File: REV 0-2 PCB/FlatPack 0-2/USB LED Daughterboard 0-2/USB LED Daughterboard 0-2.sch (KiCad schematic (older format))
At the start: 59 parts, among them J1 USB_C_Receptacle_USB2.0, J2 Conn_02x05_Odd_Even, Q1 SQJ479EP, U1 STUSB4500, U2 PCA9685PW

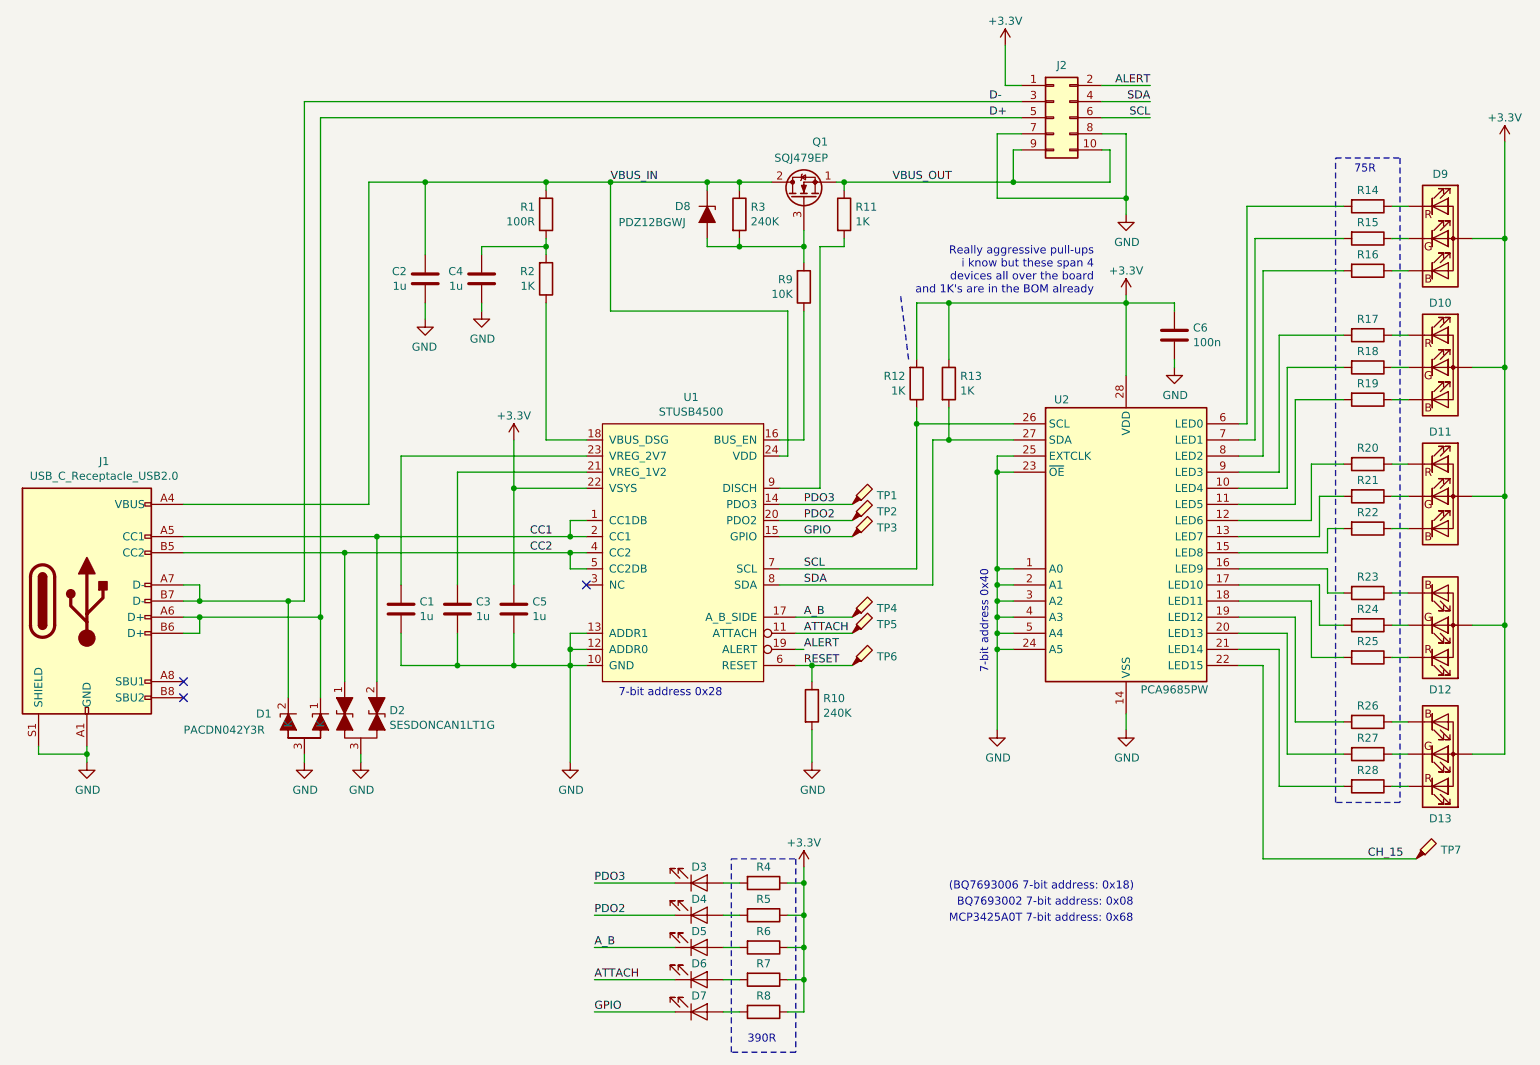
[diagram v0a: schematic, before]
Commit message: Finishing USB LED Daughterboard
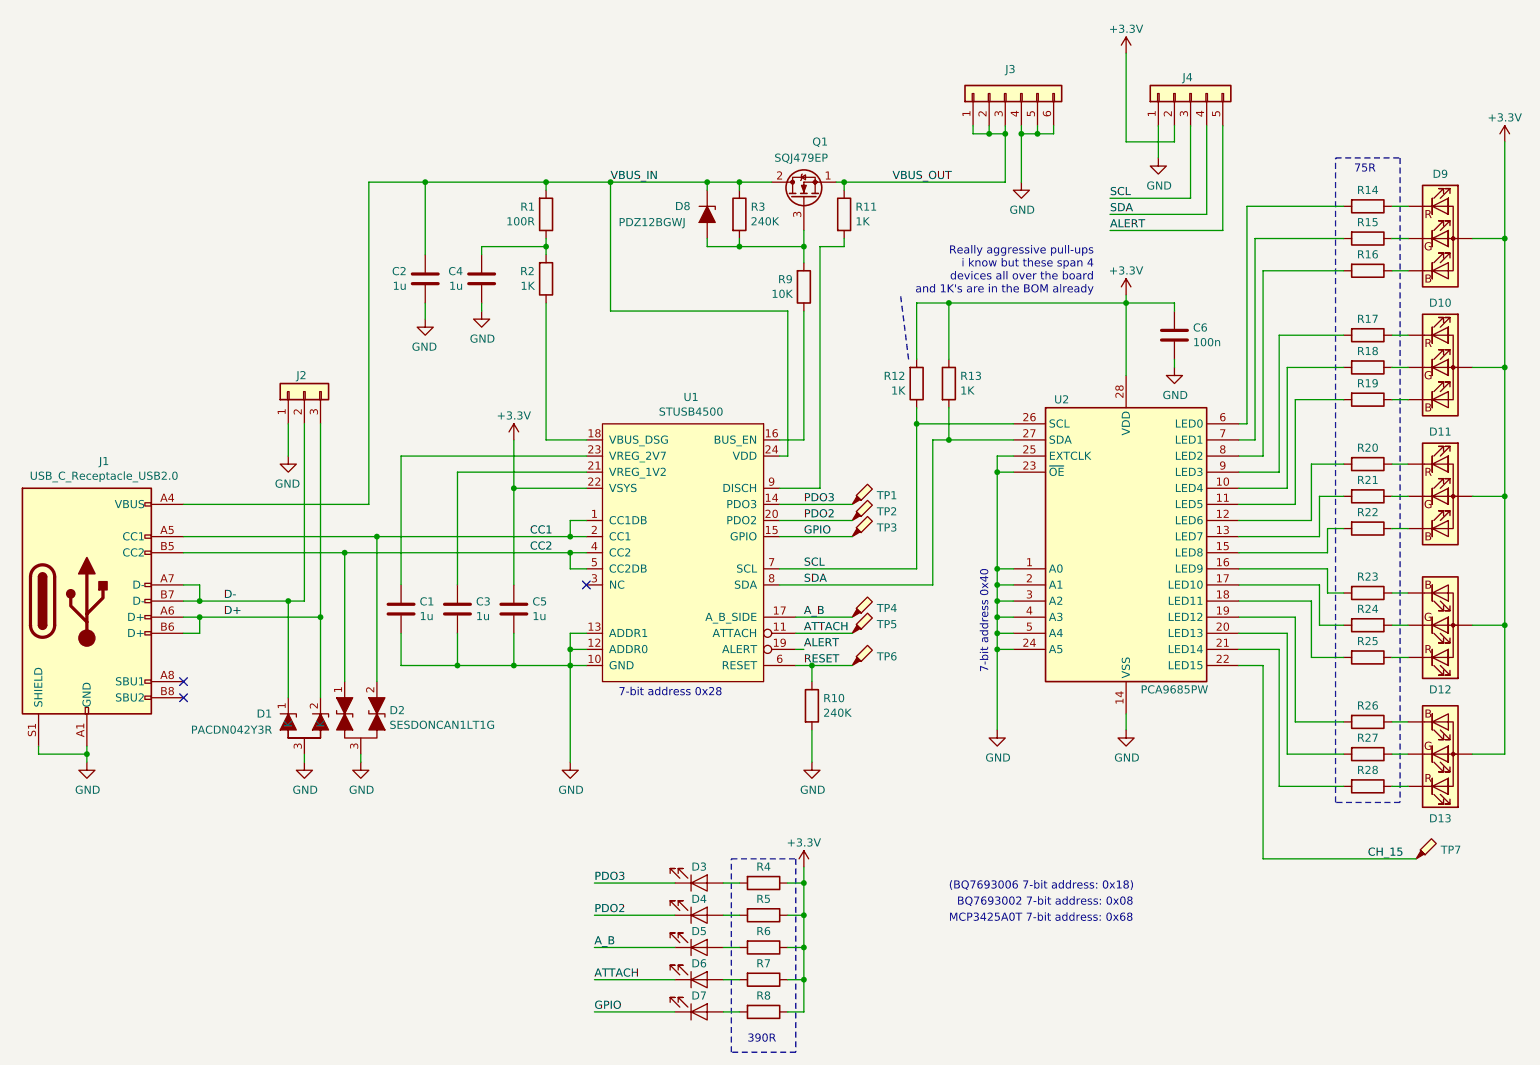
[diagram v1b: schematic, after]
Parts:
- removed J2: Conn_02x05_Odd_Even, Connector_PinHeader_2.54mm:PinHeader_2x05_P2.54mm_Vertical, symbol Connector_Generic:Conn_02x05_Odd_Even
- added J2: Conn_01x03, Connector_PinHeader_2.54mm:PinHeader_1x03_P2.54mm_Vertical, symbol Connector_Generic:Conn_01x03
- added J3: Conn_01x06, Connector_PinHeader_2.54mm:PinHeader_1x06_P2.54mm_Vertical, symbol Connector_Generic:Conn_01x06
- added J4: Conn_01x05, Connector_PinHeader_2.54mm:PinHeader_1x05_P2.54mm_Vertical, symbol Connector_Generic:Conn_01x05
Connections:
- net +3V3: now also J4.2 (Pin_2)
- net ALERT: now also J4.5 (Pin_5)
- net D+: now also D1.2 (K), J2.3 (Pin_3); no longer D1.1 (K)
- net D-: now also D1.1 (K), J2.2 (Pin_2); no longer D1.2 (K)
- net GND: now also J2.1 (Pin_1), J3.4 (Pin_4), J3.5 (Pin_5), J3.6 (Pin_6), J4.1 (Pin_1)
- net SCL: now also J4.3 (Pin_3)
- net SDA: now also J4.4 (Pin_4)
- net VBUS_OUT: now also J3.1 (Pin_1), J3.2 (Pin_2), J3.3 (Pin_3)
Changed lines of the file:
@@
 EESchema Schematic File Version 4
 LIBS:USB LED Daughterboard 0-2-cache
-EELAYER 29 0
+EELAYER 30 0
 EELAYER END
 $Descr A4 11693 8268
@@
 	2350 4700 2250 4700
 $Comp
-L power:GND #PWR03
+L power:GND #PWR04
 U 1 1 5DA9B4FB
 P 3350 5500
-F 0 "#PWR03" H 3350 5250 50  0001 C CNN
+F 0 "#PWR04" H 3350 5250 50  0001 C CNN
 F 1 "GND" H 3355 5327 50  0000 C CNN
 F 2 "" H 3350 5500 50  0001 C CNN
@@
 $EndComp
 $Comp
-L power:GND #PWR07
+L power:GND #PWR08
 U 1 1 5DA9C260
 P 4650 5500
-F 0 "#PWR07" H 4650 5250 50  0001 C CNN
+F 0 "#PWR08" H 4650 5250 50  0001 C CNN
 F 1 "GND" H 4655 5327 50  0000 C CNN
 F 2 "" H 4650 5500 50  0001 C CNN
@@
 	4500 3500 4500 2650
 $Comp
-L power:+3.3V #PWR06
+L power:+3.3V #PWR07
 U 1 1 5DA981B9
 P 4300 3500
-F 0 "#PWR06" H 4300 3350 50  0001 C CNN
+F 0 "#PWR07" H 4300 3350 50  0001 C CNN
 F 1 "+3.3V" H 4300 3650 50  0000 C CNN
 F 2 "" H 4300 3500 50  0001 C CNN
@@
 	10450 2250 10450 3050
 $Comp
-L power:+3.3V #PWR016
+L power:+3.3V #PWR018
 U 1 1 5DB37E24
 P 10450 1650
-F 0 "#PWR016" H 10450 1500 50  0001 C CNN
+F 0 "#PWR018" H 10450 1500 50  0001 C CNN
 F 1 "+3.3V" H 10450 1800 50  0000 C CNN
 F 2 "" H 10450 1650 50  0001 C CNN
@@
 CH_15
 $Comp
-L power:+3.3V #PWR013
+L power:+3.3V #PWR014
 U 1 1 5DB4EEEE
 P 8100 2600
-F 0 "#PWR013" H 8100 2450 50  0001 C CNN
+F 0 "#PWR014" H 8100 2450 50  0001 C CNN
 F 1 "+3.3V" H 8100 2750 50  0000 C CNN
 F 2 "" H 8100 2600 50  0001 C CNN
@@
 	8100 2650 8100 3100
 $Comp
-L power:GND #PWR015
+L power:GND #PWR017
 U 1 1 5DB5ADE0
 P 8400 3050
-F 0 "#PWR015" H 8400 2800 50  0001 C CNN
+F 0 "#PWR017" H 8400 2800 50  0001 C CNN
 F 1 "GND" H 8405 2877 50  0000 C CNN
 F 2 "" H 8400 3050 50  0001 C CNN
@@
 	8400 3000 8400 3050
 $Comp
-L power:GND #PWR014
+L power:GND #PWR015
 U 1 1 5DB69830
 P 8100 5300
-F 0 "#PWR014" H 8100 5050 50  0001 C CNN
+F 0 "#PWR015" H 8100 5050 50  0001 C CNN
 F 1 "GND" H 8105 5127 50  0000 C CNN
 F 2 "" H 8100 5300 50  0001 C CNN
@@
 	8100 5200 8100 5300
 $Comp
-L power:GND #PWR010
+L power:GND #PWR011
 U 1 1 5DB6DFF4
 P 7300 5300
-F 0 "#PWR010" H 7300 5050 50  0001 C CNN
+F 0 "#PWR011" H 7300 5050 50  0001 C CNN
 F 1 "GND" H 7305 5127 50  0000 C CNN
 F 2 "" H 7300 5300 50  0001 C CNN
@@
 	4100 2700 4100 2650
 $Comp
-L power:GND #PWR05
+L power:GND #PWR06
 U 1 1 5DC4C96E
 P 4100 2700
-F 0 "#PWR05" H 4100 2450 50  0001 C CNN
+F 0 "#PWR06" H 4100 2450 50  0001 C CNN
 F 1 "GND" H 4105 2527 50  0000 C CNN
 F 2 "" H 4100 2700 50  0001 C CNN
@@
 	3750 2750 3750 2650
 $Comp
-L power:GND #PWR04
+L power:GND #PWR05
 U 1 1 5DC257E0
 P 3750 2750
-F 0 "#PWR04" H 3750 2500 50  0001 C CNN
+F 0 "#PWR05" H 3750 2500 50  0001 C CNN
 F 1 "GND" H 3755 2577 50  0000 C CNN
 F 2 "" H 3750 2750 50  0001 C CNN
@@
 Wire Notes Line
 	6750 3000 6700 2600
-Text Notes 7900 2600 2    50   ~ 0
-Really aggressive pull-ups\ni know but these span 4 \ndevices all over the board\nand 1K's are in the BOM already
 $Comp
 L Device:D_Zener_ALT D8
@@
 	6150 4900 6150 5000
 $Comp
-L power:GND #PWR09
+L power:GND #PWR010
 U 1 1 5DE6D938
 P 6150 5500
-F 0 "#PWR09" H 6150 5250 50  0001 C CNN
+F 0 "#PWR010" H 6150 5250 50  0001 C CNN
 F 1 "GND" H 6155 5327 50  0000 C CNN
 F 2 "" H 6150 5500 50  0001 C CNN
@@
 U 1 1 5DF6EEEB
 P 3000 5350
-F 0 "D1" H 3300 5500 50  0000 R CNN
-F 1 "PACDN042Y3R" H 3750 5400 50  0000 R CNN
+F 0 "D1" H 2800 5500 50  0000 R CNN
+F 1 "PACDN042Y3R" H 2800 5400 50  0000 R CNN
 F 2 "Package_TO_SOT_SMD:SOT-23" H 3000 5350 50  0001 C CNN
 F 3 "https://www.onsemi.com/pub/Collateral/PACDN042-D.PDF" H 3000 5350 50  0001 C CNN
 	1    3000 5350
-	-1   0    0    -1
+	1    0    0    -1
 $EndComp
 Wire Wire Line
@@
 	3000 5500 3000 5450
 $Comp
-L power:GND #PWR02
+L power:GND #PWR03
 U 1 1 5DFAE1CC
 P 3000 5500
-F 0 "#PWR02" H 3000 5250 50  0001 C CNN
+F 0 "#PWR03" H 3000 5250 50  0001 C CNN
 F 1 "GND" H 3005 5327 50  0000 C CNN
 F 2 "" H 3000 5500 50  0001 C CNN
@@
 $EndComp
 $Comp
-L power:+3.3V #PWR08
+L power:+3.3V #PWR09
 U 1 1 5DFBA3DA
 P 6100 6150
-F 0 "#PWR08" H 6100 6000 50  0001 C CNN
+F 0 "#PWR09" H 6100 6000 50  0001 C CNN
 F 1 "+3.3V" H 6100 6300 50  0000 C CNN
 F 2 "" H 6100 6150 50  0001 C CNN
@@
 GPIO
 Wire Wire Line
-	6350 1900 7400 1900
-Connection ~ 6350 1900
-$Comp
-L Connector_Generic:Conn_02x05_Odd_Even J2
-U 1 1 5E0D0712
-P 7650 1500
-F 0 "J2" H 7700 1825 50  0000 C CNN
-F 1 "Conn_02x05_Odd_Even" H 7700 1826 50  0001 C CNN
-F 2 "Connector_PinHeader_2.54mm:PinHeader_2x05_P2.54mm_Vertical" H 7650 1500 50  0001 C CNN
-F 3 "~" H 7650 1500 50  0001 C CNN
-	1    7650 1500
-	1    0    0    -1
-$EndComp
-Wire Wire Line
-	7950 1700 8000 1700
-Wire Wire Line
-	8000 1700 8000 1900
-Wire Wire Line
-	7450 1700 7400 1700
-Wire Wire Line
-	7400 1700 7400 1900
-Connection ~ 7400 1900
-Wire Wire Line
-	7400 1900 8000 1900
-Wire Wire Line
-	7450 1600 7300 1600
-Wire Wire Line
-	7300 1600 7300 2000
-Wire Wire Line
-	7300 2000 8100 2000
-Wire Wire Line
-	8100 2000 8100 1600
-Wire Wire Line
-	8100 1600 7950 1600
-$Comp
-L power:GND #PWR012
-U 1 1 5E1029DF
-P 8100 2100
-F 0 "#PWR012" H 8100 1850 50  0001 C CNN
-F 1 "GND" H 8105 1927 50  0000 C CNN
-F 2 "" H 8100 2100 50  0001 C CNN
-F 3 "" H 8100 2100 50  0001 C CNN
-	1    8100 2100
-	1    0    0    -1
-$EndComp
-Wire Wire Line
-	8100 2000 8100 2100
-Connection ~ 8100 2000
-Wire Wire Line
-	8250 1400 7950 1400
-Wire Wire Line
-	8250 1500 7950 1500
-Wire Wire Line
-	3100 1500 7450 1500
-Wire Wire Line
-	3100 1500 3100 4600
-Wire Wire Line
-	3000 1400 7450 1400
-Wire Wire Line
-	3000 1400 3000 4500
-Text Label 7250 1500 0    50   ~ 0
-D+
-Text Label 7250 1400 0    50   ~ 0
-D-
-Text Label 8250 1400 2    50   ~ 0
-SDA
-Text Label 8250 1500 2    50   ~ 0
-SCL
-Wire Wire Line
-	8250 1300 7950 1300
-Text Label 8250 1300 2    50   ~ 0
-ALERT
-Wire Wire Line
-	7450 1300 7350 1300
-Wire Wire Line
-	7350 1300 7350 1050
-$Comp
-L power:+3.3V #PWR011
-U 1 1 5E1907B6
-P 7350 1050
-F 0 "#PWR011" H 7350 900 50  0001 C CNN
-F 1 "+3.3V" H 7350 1200 50  0000 C CNN
-F 2 "" H 7350 1050 50  0001 C CNN
-F 3 "" H 7350 1050 50  0001 C CNN
-	1    7350 1050
-	1    0    0    -1
-$EndComp
+	3100 3400 3100 4600
+Wire Wire Line
+	3000 3400 3000 4500
 $Comp
 L Device:R R15
@@
 Text Label 6650 1900 0    50   ~ 0
 VBUS_OUT
+Text Notes 7900 2600 2    50   ~ 0
+Really aggressive pull-ups\ni know but these span 4 \ndevices all over the board\nand 1K's are in the BOM already
+$Comp
+L Connector_Generic:Conn_01x03 J2
+U 1 1 5DB575F2
+P 3000 3200
+F 0 "J2" V 3100 3250 50  0000 R CNN
+F 1 "Conn_01x03" V 2873 3012 50  0001 R CNN
+F 2 "Connector_PinHeader_2.54mm:PinHeader_1x03_P2.54mm_Vertical" H 3000 3200 50  0001 C CNN
+F 3 "~" H 3000 3200 50  0001 C CNN
+	1    3000 3200
+	0    -1   -1   0
+$EndComp
+Wire Wire Line
+	2900 3400 2900 3600
+$Comp
+L power:GND #PWR02
+U 1 1 5DB6921E
+P 2900 3600
+F 0 "#PWR02" H 2900 3350 50  0001 C CNN
+F 1 "GND" H 2905 3427 50  0000 C CNN
+F 2 "" H 2900 3600 50  0001 C CNN
+F 3 "" H 2900 3600 50  0001 C CNN
+	1    2900 3600
+	-1   0    0    -1
+$EndComp
+$Comp
+L Connector_Generic:Conn_01x06 J3
+U 1 1 5DB69A33
+P 7350 1350
+F 0 "J3" V 7500 1350 50  0000 R CNN
+F 1 "Conn_01x06" V 7223 962 50  0001 R CNN
+F 2 "Connector_PinHeader_2.54mm:PinHeader_1x06_P2.54mm_Vertical" H 7350 1350 50  0001 C CNN
+F 3 "~" H 7350 1350 50  0001 C CNN
+	1    7350 1350
+	0    -1   -1   0
+$EndComp
+Wire Wire Line
+	6350 1900 7350 1900
+Wire Wire Line
+	7350 1900 7350 1600
+Connection ~ 6350 1900
+Wire Wire Line
+	7150 1550 7150 1600
+Wire Wire Line
+	7150 1600 7250 1600
+Connection ~ 7350 1600
+Wire Wire Line
+	7350 1600 7350 1550
+Wire Wire Line
+	7250 1550 7250 1600
+Connection ~ 7250 1600
+Wire Wire Line
+	7250 1600 7350 1600
+Wire Wire Line
+	7450 1550 7450 1600
+Wire Wire Line
+	7450 1600 7550 1600
+Wire Wire Line
+	7650 1600 7650 1550
+Connection ~ 7450 1600
+Wire Wire Line
+	7450 1600 7450 1900
+Wire Wire Line
+	7550 1550 7550 1600
+Connection ~ 7550 1600
+Wire Wire Line
+	7550 1600 7650 1600
+$Comp
+L power:GND #PWR012
+U 1 1 5DBCEEDC
+P 7450 1900
+F 0 "#PWR012" H 7450 1650 50  0001 C CNN
+F 1 "GND" H 7455 1727 50  0000 C CNN
+F 2 "" H 7450 1900 50  0001 C CNN
+F 3 "" H 7450 1900 50  0001 C CNN
+	1    7450 1900
+	1    0    0    -1
+$EndComp
+$Comp
+L Connector_Generic:Conn_01x05 J4
+U 1 1 5DBD11FA
+P 8500 1350
+F 0 "J4" V 8600 1400 50  0000 R CNN
+F 1 "Conn_01x05" V 8373 1062 50  0001 R CNN
+F 2 "Connector_PinHeader_2.54mm:PinHeader_1x05_P2.54mm_Vertical" H 8500 1350 50  0001 C CNN
+F 3 "~" H 8500 1350 50  0001 C CNN
+	1    8500 1350
+	0    -1   -1   0
+$EndComp
+Wire Wire Line
+	8100 1100 8100 1650
+$Comp
+L power:+3.3V #PWR013
+U 1 1 5DBF724C
+P 8100 1100
+F 0 "#PWR013" H 8100 950 50  0001 C CNN
+F 1 "+3.3V" H 8100 1250 50  0000 C CNN
+F 2 "" H 8100 1100 50  0001 C CNN
+F 3 "" H 8100 1100 50  0001 C CNN
+	1    8100 1100
+	1    0    0    -1
+$EndComp
+$Comp
+L power:GND #PWR016
+U 1 1 5DBF7880
+P 8300 1750
+F 0 "#PWR016" H 8300 1500 50  0001 C CNN
+F 1 "GND" H 8305 1577 50  0000 C CNN
+F 2 "" H 8300 1750 50  0001 C CNN
+F 3 "" H 8300 1750 50  0001 C CNN
+	1    8300 1750
+	1    0    0    -1
+$EndComp
+Wire Wire Line
+	8000 2000 8500 2000
+Wire Wire Line
+	8500 2000 8500 1550
+Wire Wire Line
+	8000 2100 8600 2100
+Wire Wire Line
+	8600 2100 8600 1550
+Wire Wire Line
+	8000 2200 8700 2200
+Wire Wire Line
+	8700 2200 8700 1550
+Text Label 8000 2200 0    50   ~ 0
+ALERT
+Text Label 8000 2000 0    50   ~ 0
+SCL
+Text Label 8000 2100 0    50   ~ 0
+SDA
+Wire Wire Line
+	8400 1650 8400 1550
+Wire Wire Line
+	8100 1650 8400 1650
+Wire Wire Line
+	8300 1550 8300 1750
+Text Label 2500 4500 0    50   ~ 0
+D-
+Text Label 2500 4600 0    50   ~ 0
+D+
 $EndSCHEMATC
